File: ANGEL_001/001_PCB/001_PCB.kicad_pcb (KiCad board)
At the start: 4 copper layers, 83.8 x 120.2 mm, 90 parts, among them J1 USB_B_Micro, J3 AudioJack3_SwitchT, SW1 SW_Push_1P1T-SH_NO_CK_KMR2xxG, SW2 SW_Push_1P1T-SH_NO_CK_KMR2xxG, U1 PCM3060, U10 USBLC6-2SC6, U11 CAP1188, U2 STM32H750VBTx, U3 LP2985-5.0, U4 PAM8302AAS, U5 IS25LP032D-JNLE, U6 TPS62172DSG, U7 BQ24072RGT, U8 MCP9700x-HTT, U9 MSA311, Y1 16MHz

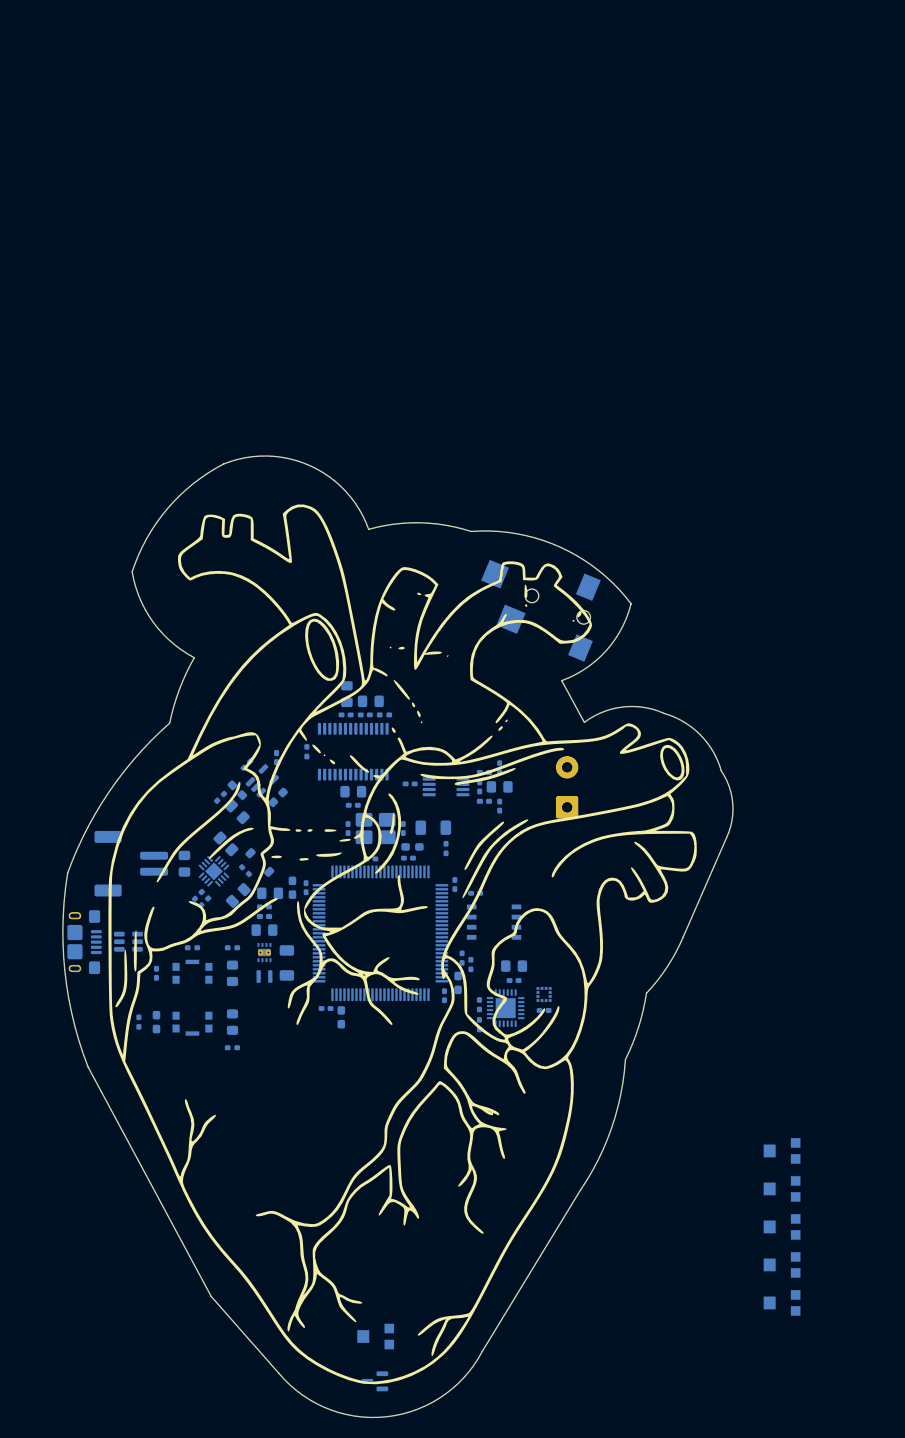
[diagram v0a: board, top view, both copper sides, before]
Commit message: PCB finalization + FSR design
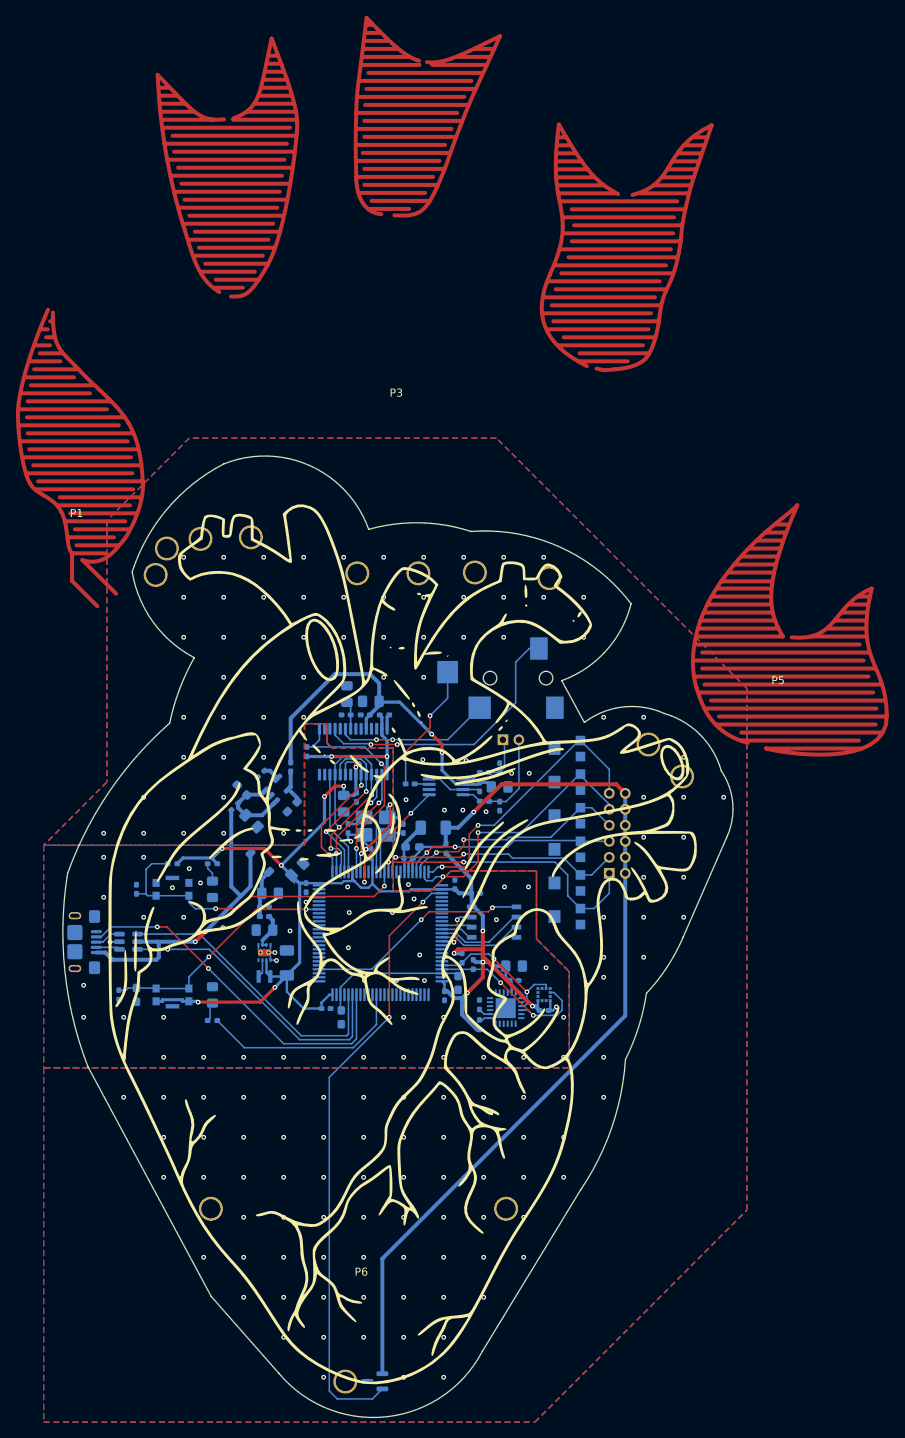
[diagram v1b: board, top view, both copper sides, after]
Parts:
- removed BT1: Battery, Connector_JST:JST_PH_S2B-PH-SM4-TB_1x02-1MP_P2.00mm_Horizontal
- removed the C34 at (91.8, 159.8)
- removed the C36 at (85.1, 155.8)
- removed the C38 at (90.3, 153.3)
- removed R12: 10k, Resistor_SMD:R_0402_1005Metric_Pad0.72x0.64mm_HandSolder
- removed the R8 at (92.7, 156.7)
- removed the R9 at (87.6, 160.6)
- removed U7: BQ24072RGT, Package_DFN_QFN:VQFN-16-1EP_3x3mm_P0.5mm_EP1.6x1.6mm
- added J2: Conn_02x06_Odd_Even, Connector_PinHeader_2.00mm:PinHeader_2x06_P2.00mm_Vertical, B.Cu at (138.2, 157.0)
- added P1: FSR_Pinky, Library:FSR_Pinky, F.Cu at (71.6, 112.5)
- added P2: FSR_Ring, Library:FSR_Ring, F.Cu at (90.4, 93.8)
- added P3: FSR_Middle, Library:FSR_Middle, F.Cu at (111.6, 97.5)
- added P4: FSR_Index, Library:FSR_Index, F.Cu at (130.5, 107.0)
- added P5: FSR_Thumb, Library:FSR_Thumb, F.Cu at (159.3, 133.4)
- added P6: FSR_Palm, Library:FSR_Palm, F.Cu at (107.2, 207.3)
- C14: value 4.7uF -> 10uF; footprint Capacitor_SMD:C_0603_1608Metric_Pad1.08x0.95mm_HandSolder -> Capacitor_SMD:C_0805_2012Metric_Pad1.18x1.45mm_HandSolder
- LS1: footprint TerminalBlock:TerminalBlock_MaiXu_MX126-5.0-02P_1x02_P5.00mm -> Connector_PinHeader_2.00mm:PinHeader_1x02_P2.00mm_Vertical
- moved RV6 77.3 mm to (132.8, 141.4)
- moved RV5 70.4 mm to (132.8, 145.6)
- moved RV4 62.3 mm to (132.8, 149.8)
- moved RV3 54.3 mm to (132.8, 154.0)
- moved RV2 46.8 mm to (132.8, 158.2)
- moved RV1 39.8 mm to (132.8, 162.4)
- moved LS1 11.7 mm to (124.9, 140.3), turned to -90 degrees
- moved C6 10.8 mm to (79.1, 159.0)
- moved D1 10.8 mm to (88.6, 159.0)
- moved R2 10.8 mm to (88.6, 155.8)
- moved R5 10.8 mm to (83.6, 155.8)
- moved SW1 10.8 mm to (83.6, 159.0)
- moved J1 9.86 mm to (127.8, 132.6), turned to 90 degrees
- moved C7 4.22 mm to (79.1, 172.2)
- moved D2 4.22 mm to (88.6, 172.2)
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- renumbered C21 to C20, C25 to C21, C26 to C22, C27 to C23, C20 to C24, C28 to C25, C22 to C26, C24 to C27, C31 to C28, C32 to C29, C33 to C30, C35 to C32, C29 to C33, C30 to C34, C37 to C36, C39 to C38, C42 to C39, FB3 to FB1, FB4 to FB2, FB1 to FB3, FB2 to FB4, J3 to J1, J1 to J3, R20 to R1, R16 to R13, R18 to R14, R19 to R15, R1 to R2, R21 to R3, R2 to R4, R3 to R5, R4 to R6, R5 to R7, R6 to R8, R7 to R9
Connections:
- C1 pad 2: GND -> GNDD
- C10 pad 2: GND -> GNDD
- C11 pad 2: GND -> GNDD
- C12 pad 2: GND -> GNDD
- C13 pad 2: GND -> GNDD
- C14 pad 2: GND -> GNDD
- C15 pad 2: GND -> GNDA
- C16 pad 2: GND -> GNDA
- C17 pad 2: GND -> GNDA
- C18 pad 2: GND -> GNDA
- C19 pad 2: GND -> GNDA
- C2 pad 2: GND -> GNDD
- C20 pad 2: GND -> GNDA
- C21 pad 2: GND -> GNDA
- C22 pad 2: GND -> GNDA
- C23 pad 2: GND -> GNDA
- C24 pad 2: GND -> GNDA
- C25 pad 2: GND -> GNDA
- C27 pad 2: GND -> GNDA
- C28 pad 2: GND -> GNDD
- C29 pad 2: GND -> GNDD
- C3 pad 1: GND -> GNDD
- C30 pad 2: GND -> GNDD
- C32 pad 2: GND -> GNDD
- C33 pad 2: GND -> GNDA
- C34 pad 2: GND -> GNDA
- C36 pad 2: GND -> GNDD
- C38 pad 2: GND -> GNDA
- C39 pad 2: GND -> GNDD
- C4 pad 2: GND -> GNDD
- C40 pad 2: GND -> GNDD
- C41 pad 2: GND -> GNDD
- C5 pad 2: GND -> GNDD
- C6 pad 2: GND -> GNDD
- C7 pad 2: GND -> GNDD
- C8 pad 1: GND -> GNDD
- C9 pad 2: GND -> GNDD
- D1 pad 1: GND -> GNDD
- D2 pad 1: GND -> GNDD
- J1 pad S: GND -> GNDA
- J3 pad 1: VBUS -> VIN
- J3 pad 5: GND -> GNDD
- R15 pad 2: GND -> GNDD
- R6 pad 2: GND -> GNDD
- RV1 pad 2: GND -> GNDA
- RV2 pad 2: GND -> GNDA
- RV3 pad 2: GND -> GNDA
- RV4 pad 2: GND -> GNDA
- RV5 pad 2: GND -> GNDA
- RV6 pad 2: GND -> GNDA
- SW1 pad 1: GND -> GNDD
- U1 pad 16: GND -> GNDD
- U1 pad 22: GND -> GNDA
- U1 pad 23: GND -> GNDA
- U1 pad 8: GND -> GNDD
- U10 pad 1: /USB_DP_IN -> /USB_DM_IN
- U10 pad 2: GND -> GNDD
- U10 pad 3: /USB_DM_IN -> /USB_DP_IN
- U10 pad 4: /USB_DM -> /USB_DP
- U10 pad 5: VBUS -> VIN
- U10 pad 6: /USB_DP -> /USB_DM
- U11 pad 10: GND -> GNDD
- U11 pad 11: GND -> GNDD
- U11 pad 12: GND -> GNDD
- U11 pad 24: GND -> GNDD
- U11 pad 25: GND -> GNDD
- U11 pad 5: GND -> GNDD
- U11 pad 6: GND -> GNDD
- U11 pad 7: GND -> GNDD
- U11 pad 8: GND -> GNDD
- U11 pad 9: GND -> GNDD
- U2 pad 10: GND -> GNDD
- U2 pad 19: GND -> GNDA
- U2 pad 26: GND -> GNDD
- U2 pad 49: GND -> GNDD
- U2 pad 74: GND -> GNDD
- U2 pad 99: GND -> GNDD
- U3 pad 2: GND -> GNDA
- U4 pad 4: GND -> GNDA
- U4 pad 7: GND -> GNDA
- U5 pad 4: GND -> GNDD
- U6 pad 1: GND -> GNDD
- U6 pad 4: GND -> GNDD
- U6 pad 5: GND -> GNDD
- U6 pad 9: GND -> GNDD
- U8 pad 3: GND -> GNDA
- U9 pad 4: GND -> GNDD
- U9 pad 8: GND -> GNDD
- U9 pad 9: GND -> GNDD
- Y1 pad 2: GND -> GNDD
- Y1 pad 4: GND -> GNDD
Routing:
- net +3.3V: track 0.00 -> 186.7 mm, vias 0 -> 14
- net +3.3VA: track 0.00 -> 121.2 mm, vias 0 -> 1
- net /TEMP_SENS: track 0.00 -> 76.3 mm, vias 0 -> 2
- net +5V: track 0.00 -> 46.2 mm, vias 0 -> 2
- net /USB_ID: track 0.00 -> 44.9 mm, vias 0 -> 2
- net VIN: track 0.00 -> 42.8 mm, vias 0 -> 2
- net /RESET: track 0.00 -> 41.3 mm, vias 0 -> 2
- net /USB_DM: track 0.00 -> 36.9 mm, vias 0 -> 2
- net /USB_DP: track 0.00 -> 36.6 mm
- net /FSR_6: track 0.00 -> 36.1 mm, vias 0 -> 2
- net /FSR_1: track 0.00 -> 36.0 mm, vias 0 -> 2
- net /AUDIO_R: track 0.00 -> 34.7 mm, vias 0 -> 2
- net /FSR_5: track 0.00 -> 34.0 mm, vias 0 -> 2
- net /FSR_2: track 0.00 -> 30.8 mm, vias 0 -> 2
- net /SAI1_FS: track 0.00 -> 30.2 mm, vias 0 -> 3
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- added copper zone on B.Cu, net GNDA
- added copper zone on F.Cu, net GNDA
- added copper zone on B.Cu, net GNDD
- added copper zone on F.Cu, net GNDD
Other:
- copper layers 4 -> 2
